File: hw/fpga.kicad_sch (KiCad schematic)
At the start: 23 parts, among them U7711 TPS7A2025PDQN, U7712 ICE40UP5K-SG48ITR, U7713 ECP5-LFE5U-12, X7701 XC8102AA01NR-G, Y7701 ECS-TXO-2016-33-400-TR

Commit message: Checkpoint. FPGA is mostly done (need a check!). Working on new LPFs. Need inductor footprints and to fix a bunch of broken/missing footprints.
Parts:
- removed C7767, C7768: 1uF, Capacitor_SMD:C_0805_2012Metric, symbol Device:C
- removed R7723: 100, Resistor_SMD:R_0603_1608Metric, symbol Device:R_US
- removed U7711: TPS7A2025PDQN, Package_SON:Texas_X2SON-4_1x1mm_P0.65mm, symbol Regulator_Linear:TPS7A20xxxDQN
- removed U7712: ICE40UP5K-SG48ITR, Package_DFN_QFN:QFN-48-1EP_7x7mm_P0.5mm_EP5.6x5.6mm, symbol Library:ICE40UP5K-SG48ITR
- removed X7701: XC8102AA01NR-G, Library:XC8102AA01NRG, symbol XC8102AA01NR-G:XC8102AA01NR-G
- added C7896, C7961, C7962, C7965, C7966, C7969: 100nF, Capacitor_SMD:C_0603_1608Metric, symbol Device:C
- added C7899, C7963: 4.7uF, Capacitor_SMD:C_0805_2012Metric, symbol Device:C
- added C7960, C7964, C7967, C7968, C7972: 10nF, Capacitor_SMD:C_0603_1608Metric, symbol Device:C
- added FB7704: 600, Inductor_SMD:L_0603_1608Metric, symbol Device:FerriteBead_Small
- added PG7709: TDO, TestPoint:TestPoint_Pad_1.0x1.0mm, symbol Connector:TestPoint_Alt
- added PG7710: TDI, TestPoint:TestPoint_Pad_1.0x1.0mm, symbol Connector:TestPoint_Alt
- added PG7711: TCK, TestPoint:TestPoint_Pad_1.0x1.0mm, symbol Connector:TestPoint_Alt
- added PG7712: TMS, TestPoint:TestPoint_Pad_1.0x1.0mm, symbol Connector:TestPoint_Alt
- added R7890, R7891: 500, Resistor_SMD:R_0603_1608Metric, symbol Device:R_Small_US
- added R7892, R7893: 4.7k, Resistor_SMD:R_0603_1608Metric, symbol Device:R_Small_US
- C7766, C7770, C7772, C7773, C7777, C7779, C7781: footprint Capacitor_SMD:C_0805_2012Metric -> Capacitor_SMD:C_0603_1608Metric
- C7769, C7771: value 4.7uF -> 100nF; footprint Capacitor_SMD:C_0805_2012Metric -> Capacitor_SMD:C_0603_1608Metric; working-voltage 10V -> 50V
- C7774: value 10nF -> 4.7uF; working-voltage 25V -> 10V
- C7775: footprint Capacitor_SMD:C_0201_0603Metric -> Capacitor_SMD:C_0603_1608Metric
- C7778, C7780: value 4.7uF -> 10nF; footprint Capacitor_SMD:C_0805_2012Metric -> Capacitor_SMD:C_0603_1608Metric; working-voltage 10V -> 25V
- Y7701: value ECS-TXO-2016-33-400-TR -> 40MHz; footprint Library:ECSTXO201633400TR -> ECSTXO201633400TR; symbol ECS-TXO-2016-33-400-TR:ECS-TXO-2016-33-400-TR -> Library:ECS-TXO-2016-33-400-TR
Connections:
- net +3.3V: now also FB7704.1; no longer C7765.1, C7766.1, Y7701.1 (TRI-STATE), Y7701.4 (VDD)
- net +3.3VFPGAIO: now also C7765.1, C7766.1, C7774.1, U7713.100 (VCCIO2), U7713.122 (VCCIO1), U7713.16 (VCCIO6), U7713.36 (VCCIO6), U7713.43 (VCCIO8), U7713.70 (VCCIO3), U7713.86 (VCCIO3), U7713.9 (VCCIO7), Y7701.1 (TRI-STATE), Y7701.4 (VDD), C7896.1, C7961.1, C7962.1, C7965.1, C7966.1, C7967.1, C7972.1, FB7704.2, R7892.1; no longer C7770.1, C7778.1, C7780.1
- net Ctrl.qsdPh0a: now also U7713.77 (PR41A)
- net Ctrl.qsdPh1a: now also U7713.81 (PR35A)
- net Ctrl.qsdPh2a: now also U7713.71 (PR47A)
- net Ctrl.qsdPh2b: now also U7713.67 (PR47B)
- net Ctrl.qsdPh2c: now also U7713.69 (PR47C)
- net Ctrl.qsdPh2d: now also U7713.68 (PR47D)
- net Ctrl.txBCLK: now also U7713.142 (PT4B)
- net Ctrl.txData: now also U7713.140 (PT9A)
- net Ctrl.txMCLK: now also U7713.143 (PT6A)
- net Ctrl.txWCLK: now also U7713.141 (PT6B)
- net FPGA.MISO: now also U7713.46 (PB11A)
- net FPGA.MOSI: now also U7713.47 (PB11B)
- net FPGA.NSS: now also U7713.48 (PB13A)
- net FPGA.SCK: now also U7713.50 (PB13B), U7713.54 (CCLK)
- net GND: now also C7771.2, C7773.2, C7774.2, C7778.1, C7780.1, U7713.32 (VSSIO6), C7896.2, C7899.2, C7960.1, C7961.2, C7962.2, C7963.2, C7964.1, C7965.2, C7966.2, C7967.2, C7968.1, C7969.2, C7972.2, R7890.2, R7891.2, R7893.2; no longer C7771.1, C7772.1, C7773.1, C7774.1, C7775.1, C7778.2, C7780.2
- net TxDrive.baseR+: now reaches U7713.24 (PL38A)
- net TxDrive.baseR-: now reaches U7713.25 (PL38B)
- net TxDrive.peakL+: now reaches U7713.28 (PL44A)
- net TxDrive.peakL-: now reaches U7713.30 (PL44B)
- net TxDrive.peakR+: now reaches U7713.31 (PL44C)
- net TxDrive.peakR-: now reaches U7713.33 (PL44D)
- net TxDrive.baseL+: now reaches U7713.34 (PL47A)
- net TxDrive.baseL-: now reaches U7713.35 (PL47B)
- net FPGACLK: now reaches U7713.37 (PL47C)
- net FPGACLK: now also Y7701.3 (OUTPUT)
- net Ctrl.qsdPh0d: now reaches U7713.73 (PR41D)
- net Ctrl.qsdPh0c: now reaches U7713.74 (PR41C)
- net Ctrl.qsdPh0b: now reaches U7713.76 (PR41B)
- net Ctrl.qsdPh1d: now reaches U7713.78 (PR35D)
- net Ctrl.qsdPh1c: now reaches U7713.79 (PR35B)
- net Ctrl.qsdPh1b: now reaches U7713.80 (PR35C)
- net +VFPGACORE: now reaches U7713.130 (VCC)
- net +VFPGACORE: now also C7772.1, C7772.2, C7775.1, C7775.2, C7778.2, C7780.2, U7713.20 (VCC), U7713.29 (VCC), U7713.38 (VCC), U7713.66 (VCC), U7713.83 (VCC), C7899.1, C7960.2, C7964.2, C7968.2
- net at U7713.132 (VCCAUX): now also C7969.1
- net at U7713.17 (VCCAUX): now also C7771.1
- net +VFPGAAUX: now reaches U7713.53 (VCCAUX)
- net +VFPGAAUX: now also C7770.1, C7963.1
- net at U7713.60 (TDO): now also PG7709.1
- net at U7713.61 (TDI): now also PG7710.1
- net at U7713.63 (TCK): now also PG7711.1
- net at U7713.64 (TMS): now also PG7712.1
- net at U7713.96 (VCCAUX): now also C7773.1
- net FPGA.INTN: now reaches U7713.55 (INITN)
- net FPGA.DONE: now reaches U7713.56 (DONE)
- net FPGA.PROG: now reaches U7713.57 (PROGRAMN)
- net FPGA.PROG: now also R7893.1
- net CFG2: now reaches U7713.58 (CFG_2)
- net CFG2: now also R7890.1
- net CFG1: now reaches U7713.59 (CFG_1)
- net CFG1: now also R7891.1
- net CFG0: now reaches U7713.62 (CFG_0)
- net CFG0: now also R7892.2
- removed net FPGA1V2: C7772.2, C7774.2, C7775.2
- no-connect marks 4 -> 2
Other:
- note added: "SSPI config mode"
- moved on the sheet: C7765, C7766, C7772, C7775, C7777, C7779, U7713A, U7713B, U7713C, U7713D, U7713E, U7713F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

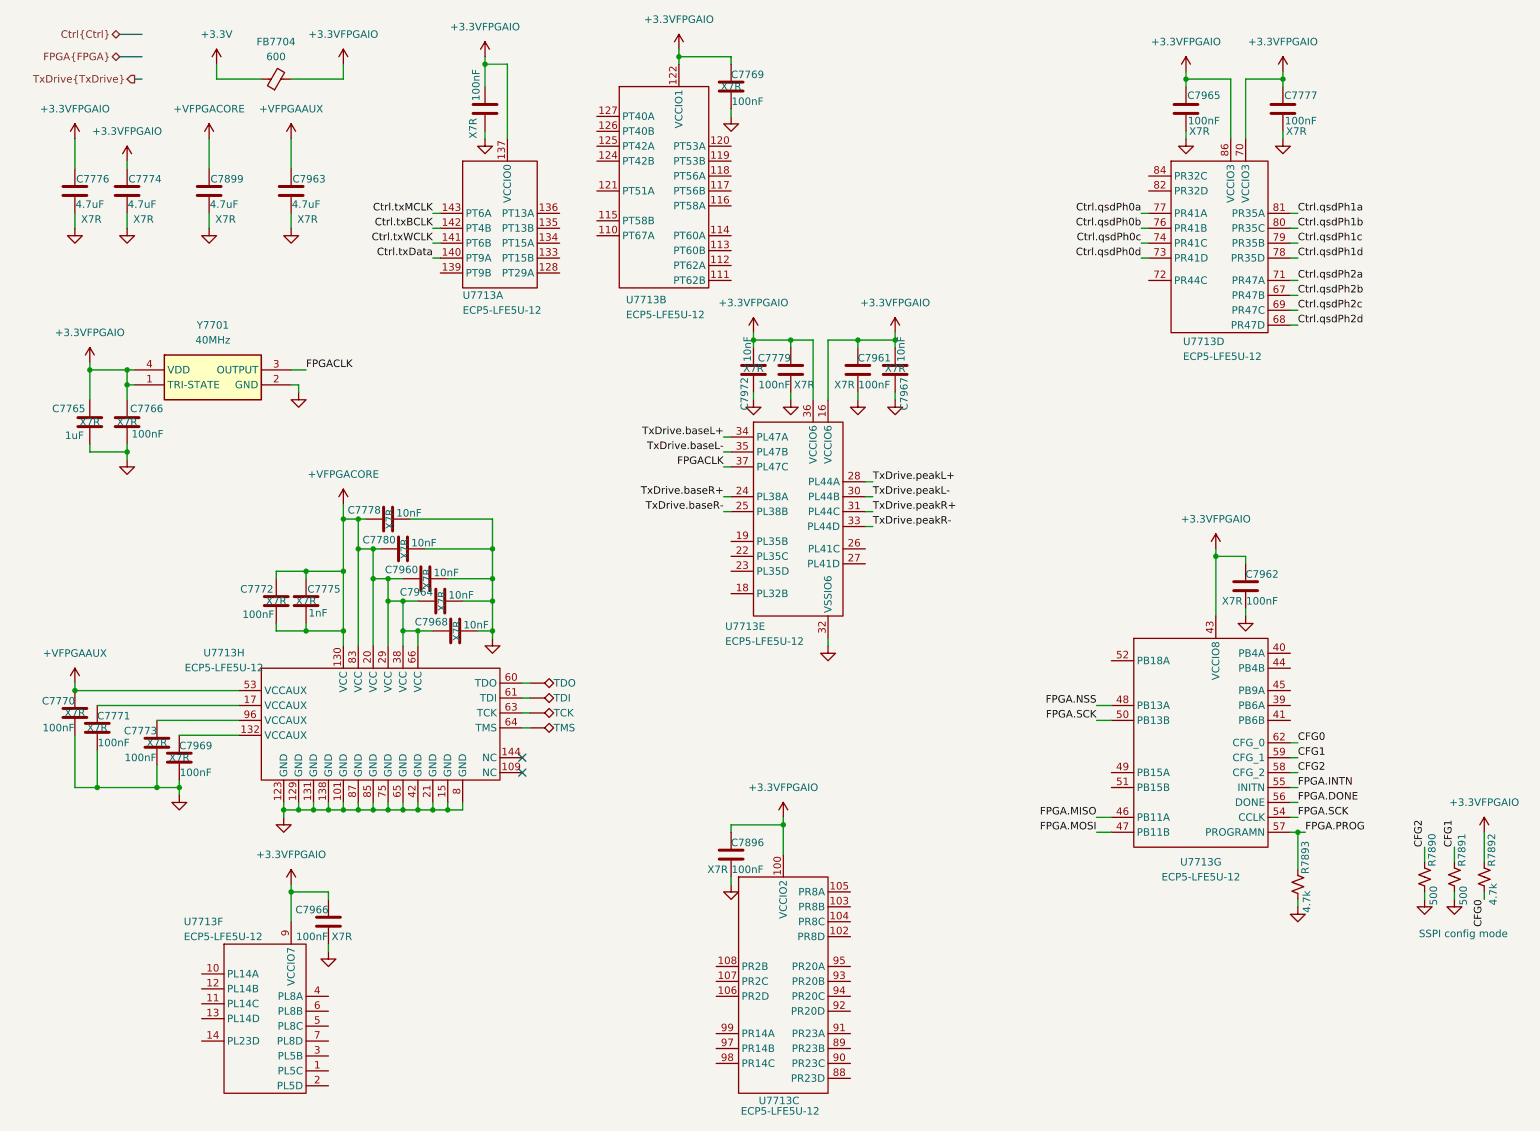
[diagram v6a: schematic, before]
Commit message: OK I have part numbers for consolidated caps, resistors, inductors and all ICs are now Uxxx refdes.
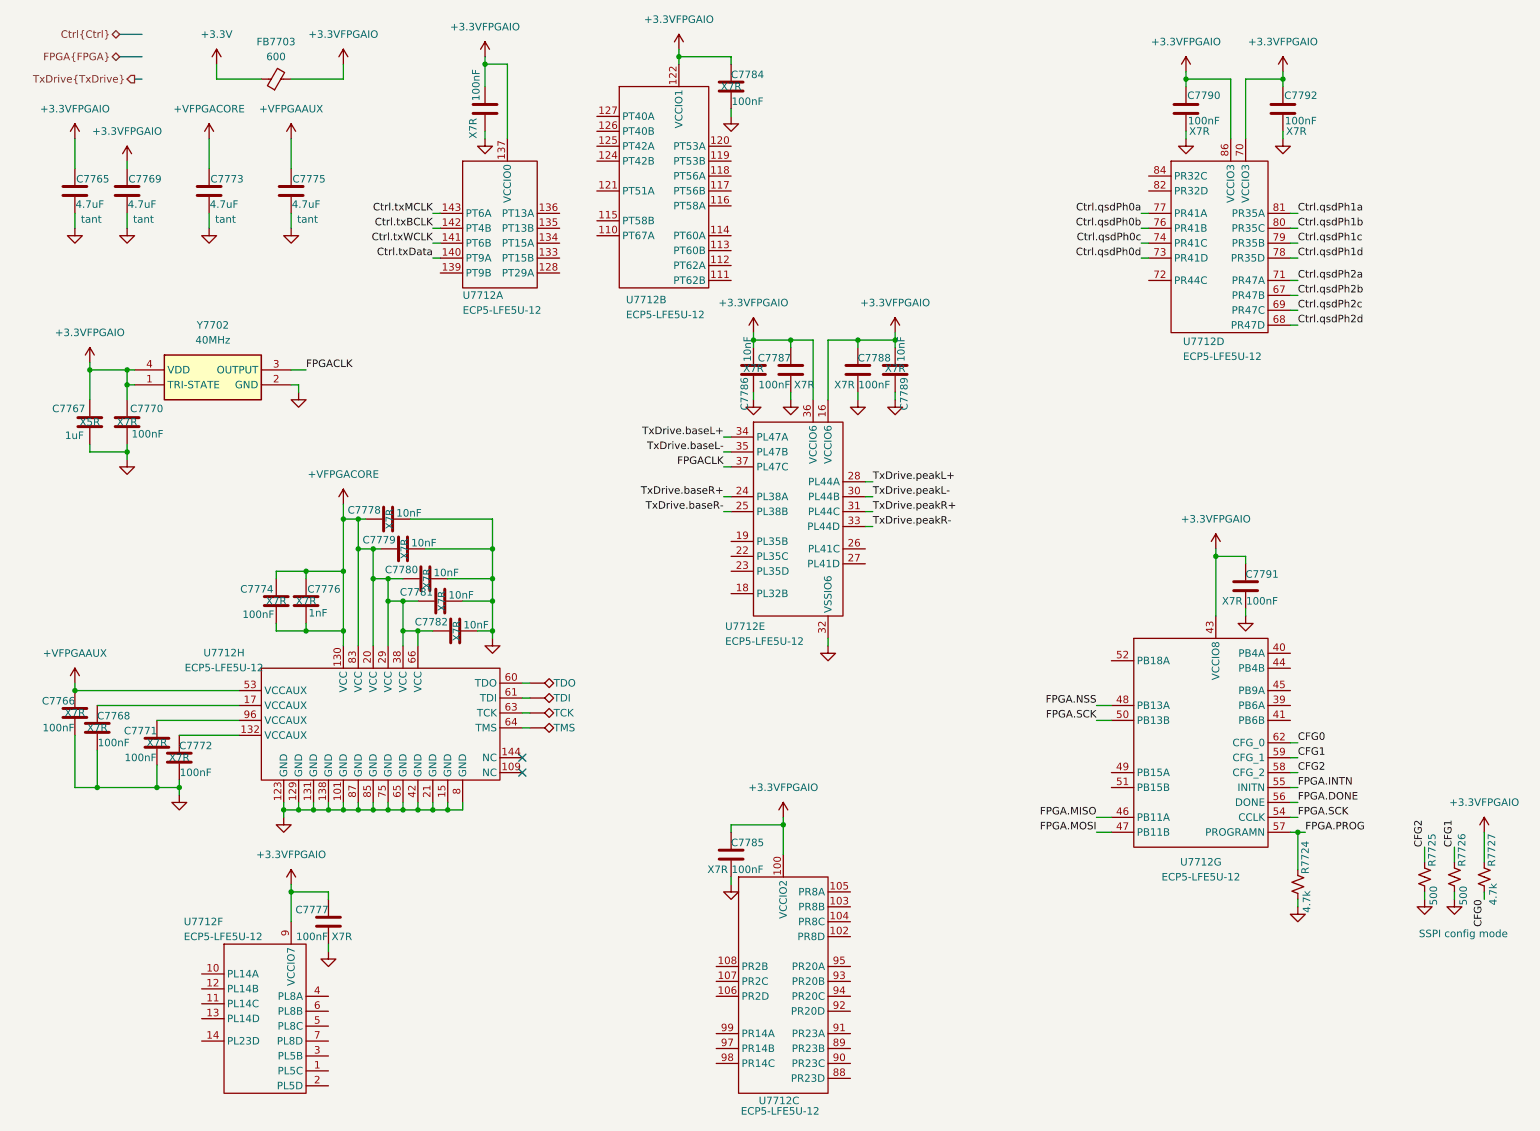
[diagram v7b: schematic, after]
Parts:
- C7765: renamed from C7776; Manufacturer_Name (none) -> Vishay/Sprague; Manufacturer_Part_Number (none) -> 298D475X9010M2T; Mouser Part Number (none) -> 74-298D475X9010M2T; cap-type X7R -> tant
- C7766: renamed from C7770; Manufacturer_Name (none) -> Kemet; Manufacturer_Part_Number (none) -> C0805F104K1RACAUTO; Mouser Part Number (none) -> 80-C0805F104K1RAUTO
- C7767: renamed from C7765; footprint Capacitor_SMD:C_0805_2012Metric -> Capacitor_SMD:C_0402_1005Metric; Manufacturer_Name (none) -> Murata; Manufacturer_Part_Number (none) -> GRM155R61E105KE11D; Mouser Part Number (none) -> 81-GRM155R61E105KE1D; cap-type X7R -> X5R; working-voltage 50V -> 25V
- C7768: renamed from C7771; Manufacturer_Name (none) -> Kemet; Manufacturer_Part_Number (none) -> C0805F104K1RACAUTO; Mouser Part Number (none) -> 80-C0805F104K1RAUTO
- C7769: renamed from C7774; Manufacturer_Name (none) -> Vishay/Sprague; Manufacturer_Part_Number (none) -> 298D475X9010M2T; Mouser Part Number (none) -> 74-298D475X9010M2T; cap-type X7R -> tant
- C7770: renamed from C7766; Manufacturer_Name (none) -> Kemet; Manufacturer_Part_Number (none) -> C0805F104K1RACAUTO; Mouser Part Number (none) -> 80-C0805F104K1RAUTO
- C7771: renamed from C7773; Manufacturer_Name (none) -> Kemet; Manufacturer_Part_Number (none) -> C0805F104K1RACAUTO; Mouser Part Number (none) -> 80-C0805F104K1RAUTO
- C7772: renamed from C7969; Manufacturer_Name (none) -> Kemet; Manufacturer_Part_Number (none) -> C0805F104K1RACAUTO; Mouser Part Number (none) -> 80-C0805F104K1RAUTO
- C7773: renamed from C7899; Manufacturer_Name (none) -> Vishay/Sprague; Manufacturer_Part_Number (none) -> 298D475X9010M2T; Mouser Part Number (none) -> 74-298D475X9010M2T; cap-type X7R -> tant
- C7774: renamed from C7772; Manufacturer_Name (none) -> Kemet; Manufacturer_Part_Number (none) -> C0805F104K1RACAUTO; Mouser Part Number (none) -> 80-C0805F104K1RAUTO
- C7775: renamed from C7963; Manufacturer_Name (none) -> Vishay/Sprague; Manufacturer_Part_Number (none) -> 298D475X9010M2T; Mouser Part Number (none) -> 74-298D475X9010M2T; cap-type X7R -> tant
- C7776: renamed from C7775; Manufacturer_Name (none) -> Kyocera AVX; Manufacturer_Part_Number (none) -> KAF15AR71H102KM; Mouser Part Number (none) -> 581-KAF15AR71H102KM
- C7777: renamed from C7966; Manufacturer_Name (none) -> Kemet; Manufacturer_Part_Number (none) -> C0805F104K1RACAUTO; Mouser Part Number (none) -> 80-C0805F104K1RAUTO
- C7778: Manufacturer_Name (none) -> Murata; Manufacturer_Part_Number (none) -> GCM1885C2A103JE02J; Mouser Part Number (none) -> 81-GCM1885C2A103JE2J
- C7779: renamed from C7780; Manufacturer_Name (none) -> Murata; Manufacturer_Part_Number (none) -> GCM1885C2A103JE02J; Mouser Part Number (none) -> 81-GCM1885C2A103JE2J
- C7780: renamed from C7960; Manufacturer_Name (none) -> Murata; Manufacturer_Part_Number (none) -> GCM1885C2A103JE02J; Mouser Part Number (none) -> 81-GCM1885C2A103JE2J
- C7781: renamed from C7964; Manufacturer_Name (none) -> Murata; Manufacturer_Part_Number (none) -> GCM1885C2A103JE02J; Mouser Part Number (none) -> 81-GCM1885C2A103JE2J
- C7782: renamed from C7968; Manufacturer_Name (none) -> Murata; Manufacturer_Part_Number (none) -> GCM1885C2A103JE02J; Mouser Part Number (none) -> 81-GCM1885C2A103JE2J
- C7783: renamed from C7781; Manufacturer_Name (none) -> Kemet; Manufacturer_Part_Number (none) -> C0805F104K1RACAUTO; Mouser Part Number (none) -> 80-C0805F104K1RAUTO
- C7784: renamed from C7769; Manufacturer_Name (none) -> Kemet; Manufacturer_Part_Number (none) -> C0805F104K1RACAUTO; Mouser Part Number (none) -> 80-C0805F104K1RAUTO
- C7785: renamed from C7896; Manufacturer_Name (none) -> Kemet; Manufacturer_Part_Number (none) -> C0805F104K1RACAUTO; Mouser Part Number (none) -> 80-C0805F104K1RAUTO
- C7786: renamed from C7972; Manufacturer_Name (none) -> Murata; Manufacturer_Part_Number (none) -> GCM1885C2A103JE02J; Mouser Part Number (none) -> 81-GCM1885C2A103JE2J
- C7787: renamed from C7779; Manufacturer_Name (none) -> Kemet; Manufacturer_Part_Number (none) -> C0805F104K1RACAUTO; Mouser Part Number (none) -> 80-C0805F104K1RAUTO
- C7788: renamed from C7961; Manufacturer_Name (none) -> Kemet; Manufacturer_Part_Number (none) -> C0805F104K1RACAUTO; Mouser Part Number (none) -> 80-C0805F104K1RAUTO
- C7789: renamed from C7967; Manufacturer_Name (none) -> Murata; Manufacturer_Part_Number (none) -> GCM1885C2A103JE02J; Mouser Part Number (none) -> 81-GCM1885C2A103JE2J
- C7790: renamed from C7965; Manufacturer_Name (none) -> Kemet; Manufacturer_Part_Number (none) -> C0805F104K1RACAUTO; Mouser Part Number (none) -> 80-C0805F104K1RAUTO
- C7791: renamed from C7962; Manufacturer_Name (none) -> Kemet; Manufacturer_Part_Number (none) -> C0805F104K1RACAUTO; Mouser Part Number (none) -> 80-C0805F104K1RAUTO
- C7792: renamed from C7777; Manufacturer_Name (none) -> Kemet; Manufacturer_Part_Number (none) -> C0805F104K1RACAUTO; Mouser Part Number (none) -> 80-C0805F104K1RAUTO
- renumbered FB7704 to FB7703, R7893 to R7724, R7890 to R7725, R7891 to R7726, R7892 to R7727, U7713 to U7712, Y7701 to Y7702
